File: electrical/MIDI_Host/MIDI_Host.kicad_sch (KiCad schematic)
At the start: 4 parts, among them CN1 USB-CON-AF-LCP-Offset, SW1 ST-0-102-C03-N003-RS, SW2 TC-1109DE-C-G, U8 ESP32-WROOM-32U

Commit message: SUKU sch done
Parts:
- removed U8: ESP32-WROOM-32U, RF_Module:ESP32-WROOM-32U, symbol RF_Module:ESP32-WROOM-32U
- added C15: (no value), suku_basics:CAP_0805, symbol suku_basics:CAP
- added C16: 100n, suku_basics:CAP_0805, symbol suku_basics:CAP
- added C17: 1u, suku_basics:CAP_0805, symbol suku_basics:CAP
- added D10, D8, D9: (no value), symbol suku_basics:UI_WS2812C-2020
- added J1: USB_C_TYPE-C-32-M-12, suku_basics:USB_C_Korean_Hroparts_TYPE-C-31-M-12, symbol suku_basics:USB_C_TYPE-C-32-M-12
- added J2: (NF), Connector_PinHeader_1.27mm:PinHeader_2x05_P1.27mm_Vertical, symbol Connector_Generic:Conn_02x05_Odd_Even
- added R10, R11, R18, R19: 1k, suku_basics:RES_0805, symbol suku_basics:RES
- added R12, R9: (no value), suku_basics:RES_0805, symbol suku_basics:RES
- added R13, R14, R16: 5k1, suku_basics:RES_0805, symbol suku_basics:RES
- added U11, U12: (no value), suku_basics:SOT-363_SC-70-6, symbol suku_basics:BL1551B
- added U13: LN1134A332MR-G, suku_basics:SOT-23-5, symbol suku_basics:U_REGULATOR_SOT23-5
- added U14: (no value), suku_basics:SOT-23-6, symbol suku_basics:U_ESD_4ch
- added U15: SESRV05-4, suku_basics:SOT-23-6, symbol suku_basics:U_ESD_4ch
- added U4: (no value), suku_basics:ESP32-S3-WROOM-1U, symbol suku_basics:ESP32-S3-WROOM-1U
- SW1: value ST-0-102-C03-N003-RS -> (none)
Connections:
- net +3V3: now reaches SW1.1
- net +3V3: now also J2.1 (Pin_1), R16.1, U13.5 (OUT), U4.2 (VDD)
- net at SW1.2: now also R10.2
- net GND: now reaches SW1.3
- net GND: now also CN1.4 (GND), CN1.SH1, CN1.SH2, SW2.2, SW2.3, C15.2, C16.2, C17.2, D10.2 (VSS), D8.2 (VSS), D9.2 (VSS), J1.A12B1 (GND), J1.A1B12 (GND), J2.3 (Pin_3), J2.5 (Pin_5), R13.2, R14.2, R19.2, U11.2 (GND), U12.2 (GND), U13.2 (GND), U14.2, U15.2, U4.1 (GND), U4.40 (GND), U4.41 (GND_PAD)
- net at SW2.1: now also R9.2
- net VBUS: now reaches CN1.1 (VCC)
- net CONN_A_D-: now reaches CN1.2 (D-)
- net CONN_A_D-: now also U12.3 (A2), U15.1, U15.3
- net CONN_A_D+: now reaches CN1.3 (D+)
- net CONN_A_D+: now also U11.3 (A2), U15.4, U15.6
- new net: J2.7 (Pin_7), R18.1
- new net: D8.3 (DIN), R11.2, R12.1
- new net: R19.1, U4.15 (GPIO3)
- new net: R16.2, U4.3 (EN)
- new net: D10.3 (DIN), D9.1 (DOUT)
- new net: D8.1 (DOUT), D9.3 (DIN)
- new net: J1.A5 (CC1), R14.1
- new net: J1.B5 (CC2), R13.1
- new net +5V: C17.1, D10.4 (VDD), D8.4 (VDD), D9.4 (VDD), J1.A4B9 (VBUS), J1.A9B4 (VBUS), R12.2, U11.5 (VCC), U12.5 (VCC), U13.1 (IN), U13.3 (EN), U14.5, U15.5
- new net CONN_C_D+: J1.A6 (D+), J1.B6 (D+), U11.1 (A1), U14.4, U14.6
- new net CONN_C_D-: J1.A7 (D-), J1.B7 (D-), U12.1 (A1), U14.1, U14.3
- new net LED_DATA: R11.1, U4.39 (GPIO1)
- new net MCU_D+: U11.4 (B), U4.14 (GPIO20/USB_D+)
- new net MCU_D-: U12.4 (B), U4.13 (GPIO19/USB_D-)
- new net MIDI_UART_RX: U4.11 (GPIO18)
- new net MIDI_UART_TX: U4.10 (GPIO17)
- new net SW_AB: C16.1, R10.1, U4.28 (GPIO35)
- new net SW_BOOT: C15.1, R9.1, U4.27 (GPIO0)
- new net TCK: J2.4 (Pin_4), U4.32 (GPIO39/MTCK)
- new net TDI: J2.8 (Pin_8), U4.34 (GPIO41/MTDI)
- new net TDO: J2.6 (Pin_6), U4.33 (GPIO40/MTDO)
- new net TMS: J2.2 (Pin_2), U4.35 (GPIO42/MTMS)
- new net TRS_TYPE_SELECT: U4.9 (GPIO16)
- new net U0RXD: J2.9 (Pin_9), U4.36 (GPIO44/U0RXD)
- new net U0TXD: R18.2, U4.37 (GPIO43/U0TXD)
- new net USB_SELECT: U11.6 (ENB), U12.6 (ENB), U4.12 (GPIO8)
- no-connect marks 17 -> 30
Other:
- moved on the sheet: CN1, SW1, SW2

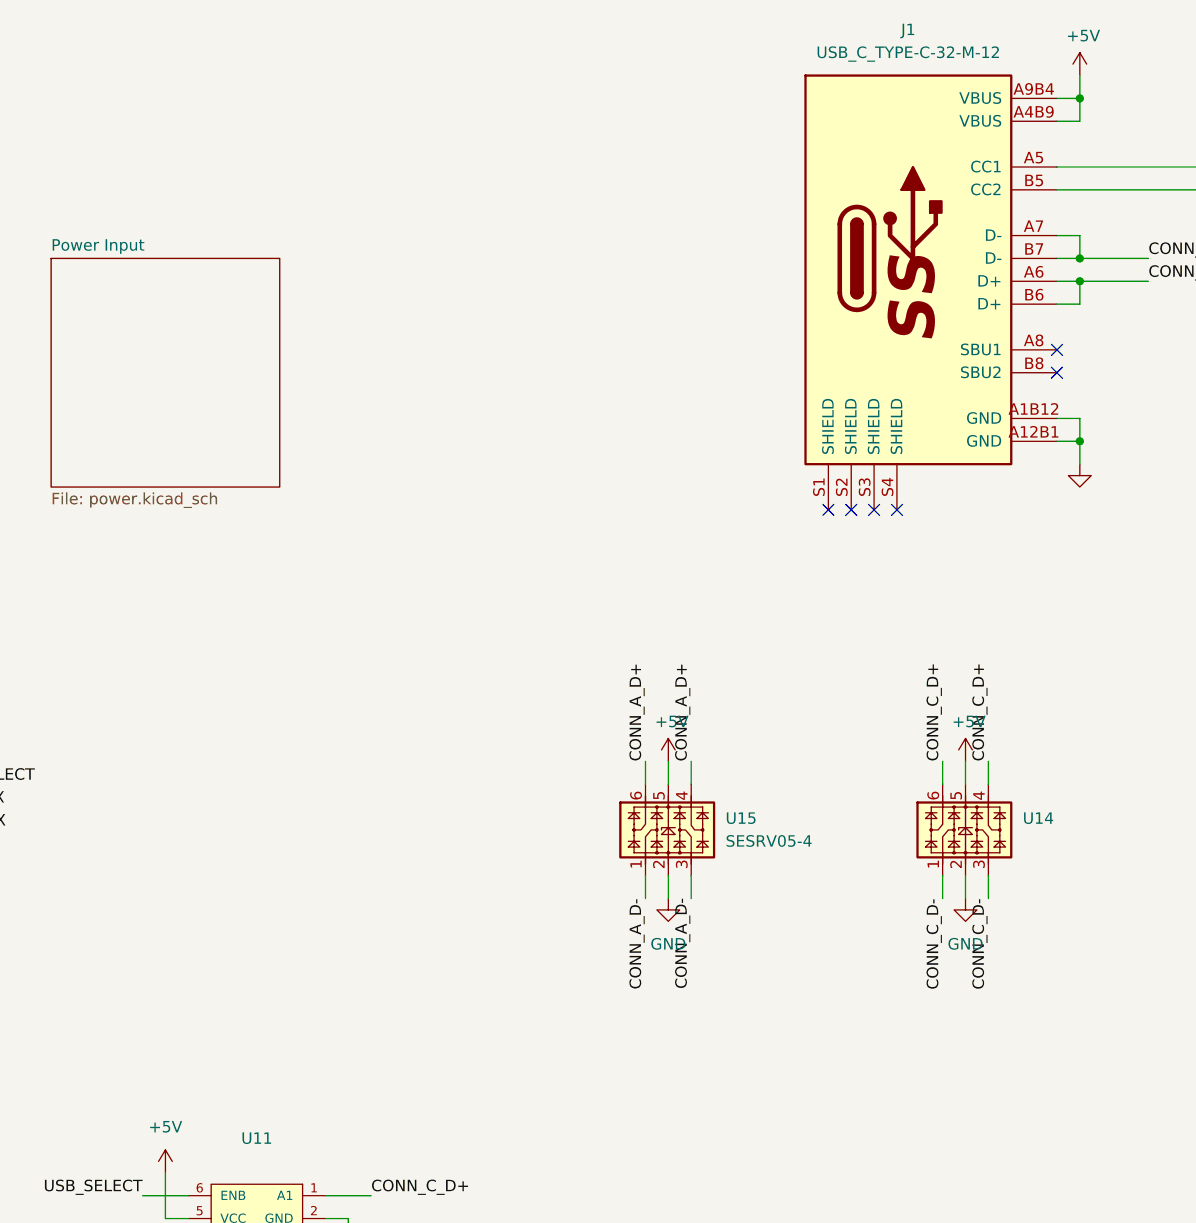
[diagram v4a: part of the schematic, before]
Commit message: SUKU tht components included in pos file
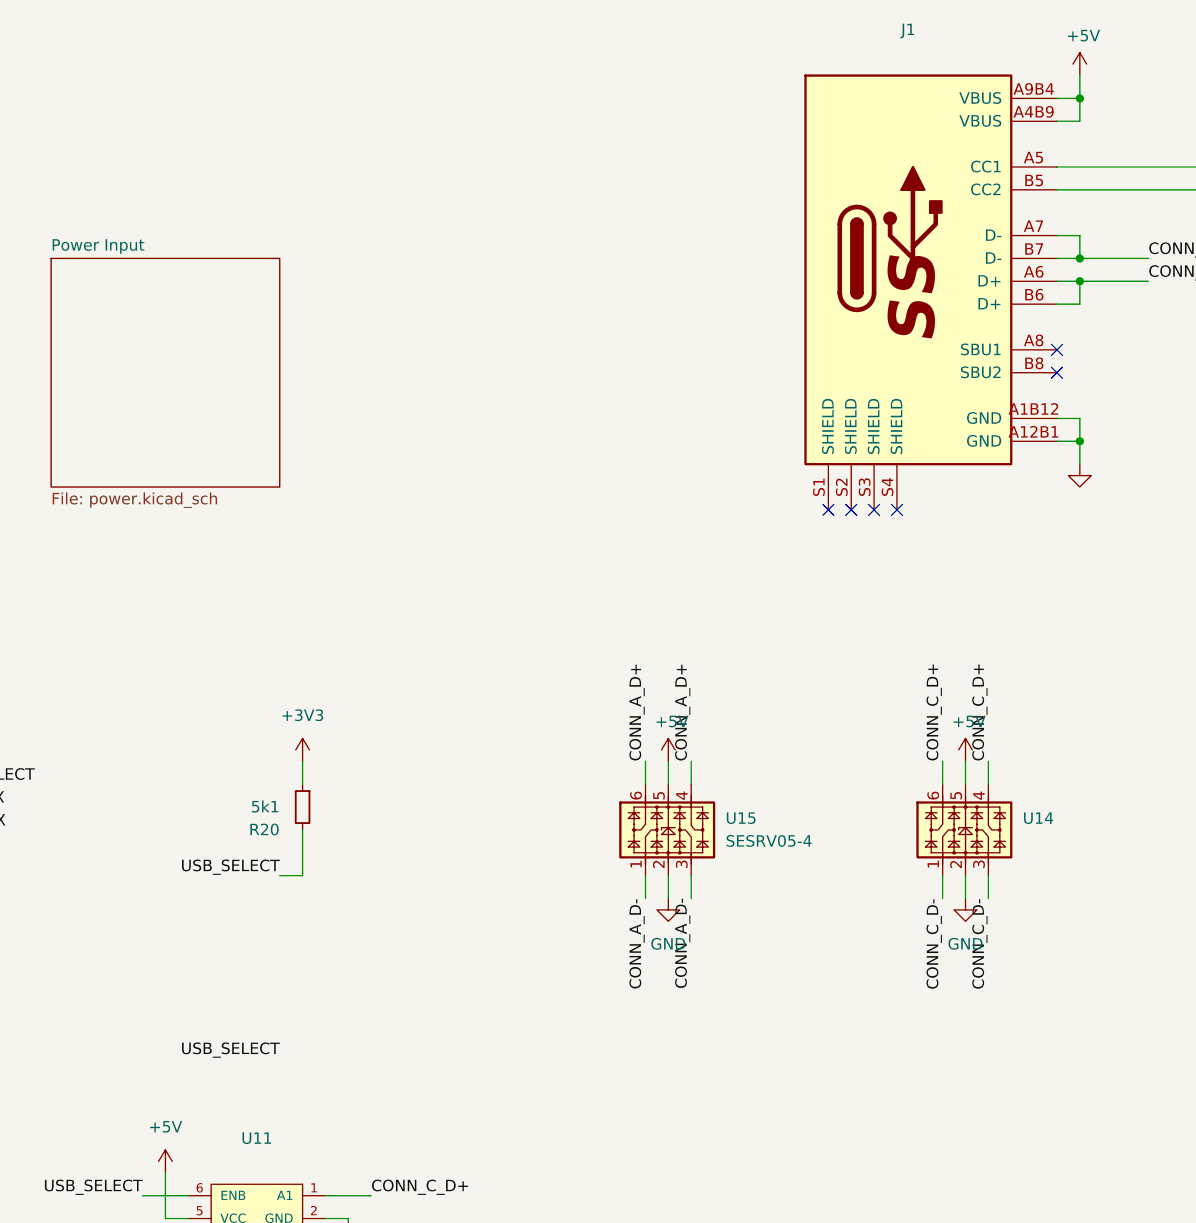
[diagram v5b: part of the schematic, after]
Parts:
- added R20: 5k1, suku_basics:RES_0805, symbol suku_basics:RES
- J1: value USB_C_TYPE-C-32-M-12 -> (none)
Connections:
- net +3V3: now also R20.1
- net USB_SELECT: now also R20.2
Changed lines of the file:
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@@
   (no_connect (at 55.88 165.1))
   (no_connect (at 55.88 182.88))
+  (no_connect (at 55.88 99.06))
+  (no_connect (at 55.88 96.52))
+  (no_connect (at 55.88 101.6))
+  (no_connect (at 55.88 104.14))
+  (no_connect (at 55.88 106.68))
+  (no_connect (at 55.88 144.78))
+  (no_connect (at 55.88 147.32))
+  (no_connect (at 55.88 137.16))
   (no_connect (at 55.88 142.24))
   (no_connect (at 55.88 139.7))
@@
   (no_connect (at 55.88 129.54))
   (no_connect (at 55.88 127))
-  (no_connect (at 55.88 99.06))
-  (no_connect (at 55.88 96.52))
-  (no_connect (at 55.88 101.6))
-  (no_connect (at 55.88 144.78))
-  (no_connect (at 55.88 147.32))
-  (no_connect (at 55.88 137.16))
-  (no_connect (at 55.88 104.14))
-  (no_connect (at 55.88 106.68))
   (no_connect (at 162.56 256.54))
   (no_connect (at 170.18 78.74))
@@
     (stroke (width 0) (type default) (color 0 0 0 0))
   )
+  (wire (pts (xy 101.6 119.38) (xy 104.14 119.38))
+    (stroke (width 0) (type default) (color 0 0 0 0))
+  )
   (wire (pts (xy 20.32 160.02) (xy 20.32 157.48))
     (stroke (width 0) (type default) (color 0 0 0 0))
@@
     (stroke (width 0) (type default) (color 0 0 0 0))
   )
+  (wire (pts (xy 104.14 106.68) (xy 104.14 109.22))
+    (stroke (width 0) (type default) (color 0 0 0 0))
+  )
   (wire (pts (xy 175.26 106.68) (xy 175.26 109.22))
     (stroke (width 0) (type default) (color 0 0 0 0))
@@
   )
   (wire (pts (xy 254 104.14) (xy 266.7 104.14))
+    (stroke (width 0) (type default) (color 0 0 0 0))
+  )
+  (wire (pts (xy 104.14 119.38) (xy 104.14 114.3))
     (stroke (width 0) (type default) (color 0 0 0 0))
   )
@@
     (effects (font (size 1.27 1.27)) (justify left bottom))
   )
+  (label "USB_SELECT" (at 101.6 139.7 180)
+    (effects (font (size 1.27 1.27)) (justify right bottom))
+  )
   (label "CONN_C_D-" (at 111.76 170.18 0)
     (effects (font (size 1.27 1.27)) (justify left bottom))
@@
   )
   (label "TDI" (at 119.38 208.28 180)
+    (effects (font (size 1.27 1.27)) (justify right bottom))
+  )
+  (label "USB_SELECT" (at 101.6 119.38 180)
     (effects (font (size 1.27 1.27)) (justify right bottom))
   )
@@
     (pin "6")
   )
+  (symbol (lib_id "suku_basics:RES") (at 104.14 111.76 0) (mirror y) (unit 1)
+    (in_bom yes) (on_board yes)
+    (property "Reference" "R20" (id 0) (at 101.6 114.3 0)
+      (effects (font (size 1.27 1.27)) (justify left))
+    )
+    (property "Value" "5k1" (id 1) (at 101.6 111.76 0)
+      (effects (font (size 1.27 1.27)) (justify left))
+    )
+    (property "Footprint" "suku_basics:RES_0805" (id 2) (at 104.14 111.76 0)
+      (effects (font (size 1.27 1.27)) hide)
+    )
+    (property "Datasheet" "~" (id 3) (at 104.14 111.76 0)
+      (effects (font (size 1.27 1.27)) hide)
+    )
+    (pin "1")
+    (pin "2")
+  )
   (symbol (lib_id "power:+3V3") (at 20.32 86.36 0) (unit 1)
     (in_bom yes) (on_board yes) (fields_autoplaced)
@@
     (in_bom yes) (on_board yes) (fields_autoplaced)
     (property "Reference" "J1" (id 0) (at 171.45 25.4 0))
-    (property "Value" "USB_C_TYPE-C-32-M-12" (id 1) (at 171.45 27.94 0))
+    (property "Value" "" (id 1) (at 171.45 27.94 0))
     (property "Footprint" "suku_basics:USB_C_Korean_Hroparts_TYPE-C-31-M-12" (id 2) (at 172.72 50.8 0)
       (effects (font (size 1.27 1.27)) hide)
@@
     (pin "1")
   )
+  (symbol (lib_id "power:+3V3") (at 104.14 106.68 0) (unit 1)
+    (in_bom yes) (on_board yes) (fields_autoplaced)
+    (property "Reference" "#PWR0155" (id 0) (at 104.14 110.49 0)
+      (effects (font (size 1.27 1.27)) hide)
+    )
+    (property "Value" "+3V3" (id 1) (at 104.14 101.6 0))
+    (property "Footprint" "" (id 2) (at 104.14 106.68 0)
+      (effects (font (size 1.27 1.27)) hide)
+    )
+    (property "Datasheet" "" (id 3) (at 104.14 106.68 0)
+      (effects (font (size 1.27 1.27)) hide)
+    )
+    (pin "1")
+  )
   (symbol (lib_id "power:GND") (at 139.7 218.44 0) (unit 1)
     (in_bom yes) (on_board yes)
@@
       (reference "#PWR0154") (unit 1) (value "GND") (footprint "")
     )
+    (path "/de7a4db3-4abd-4376-9939-f04f8af92c47"
+      (reference "#PWR0155") (unit 1) (value "+3V3") (footprint "")
+    )
     (path "/b46fd59b-d980-4e81-961e-66caead0767c"
       (reference "#PWR0161") (unit 1) (value "+5V") (footprint "")
@@
     )
     (path "/a2a8c99d-0466-4790-bd7a-1670453815fe"
-      (reference "J1") (unit 1) (value "USB_C_TYPE-C-32-M-12") (footprint "suku_basics:USB_C_Korean_Hroparts_TYPE-C-31-M-12")
+      (reference "J1") (unit 1) (value "MC-107DM") (footprint "suku_basics:USB_C_Korean_Hroparts_TYPE-C-31-M-12")
     )
     (path "/ad772e68-bc9b-430b-a352-88e784b93e97"
@@
       (reference "R19") (unit 1) (value "1k") (footprint "suku_basics:RES_0805")
     )
+    (path "/690e61dd-19d9-4427-95a8-e6177bc29906"
+      (reference "R20") (unit 1) (value "5k1") (footprint "suku_basics:RES_0805")
+    )
     (path "/7a90775c-1fe6-4f36-9f90-6ac91a02dbe1"
